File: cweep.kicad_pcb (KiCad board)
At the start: 2 copper layers, 35 parts, among them SW1 SW_Push, SW10 SW_Push, SW11 SW_Push, SW12 SW_Push, SW13 SW_Push, SW14 SW_Push, SW15 SW_Push, SW16 SW_Push, SW17 SW_Push, SW2 SW_Push, SW3 SW_Push, SW4 SW_Push, SW5 SW_Push, SW6 SW_Push, SW7 SW_Push, SW8 SW_Push, SW9 SW_Push, U1 XIAO-nRF52840

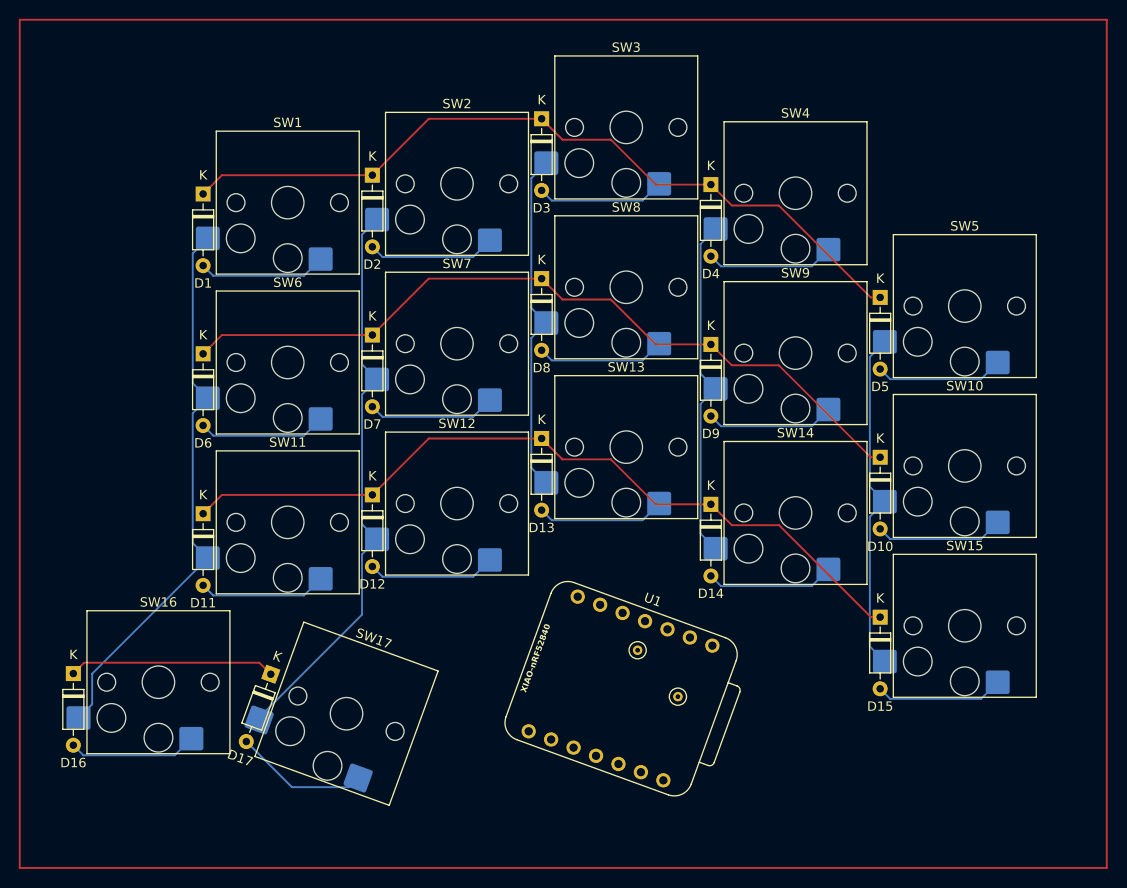
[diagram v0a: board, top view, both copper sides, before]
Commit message: refactor: update footprints
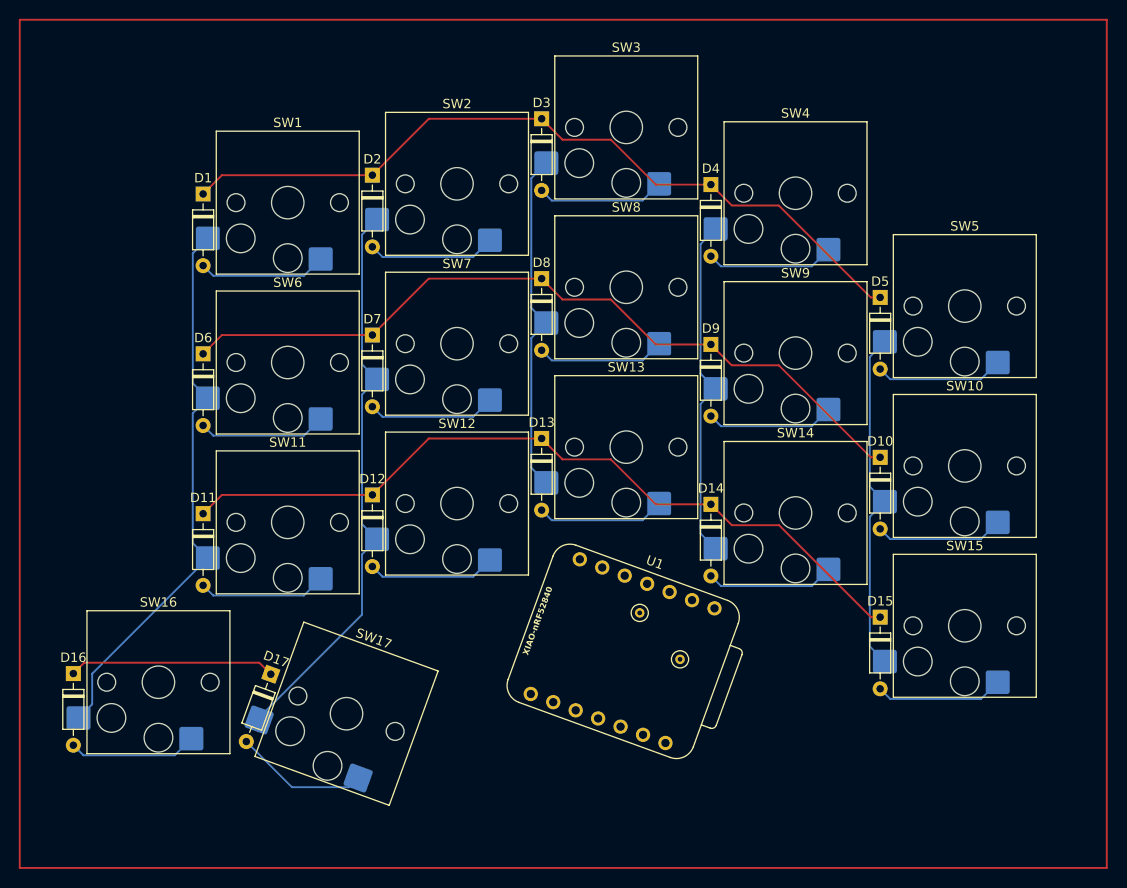
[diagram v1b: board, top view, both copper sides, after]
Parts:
- moved U1 3.98 mm to (222.6, 98.8)

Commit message: feat: add matrix-to-mcu routes
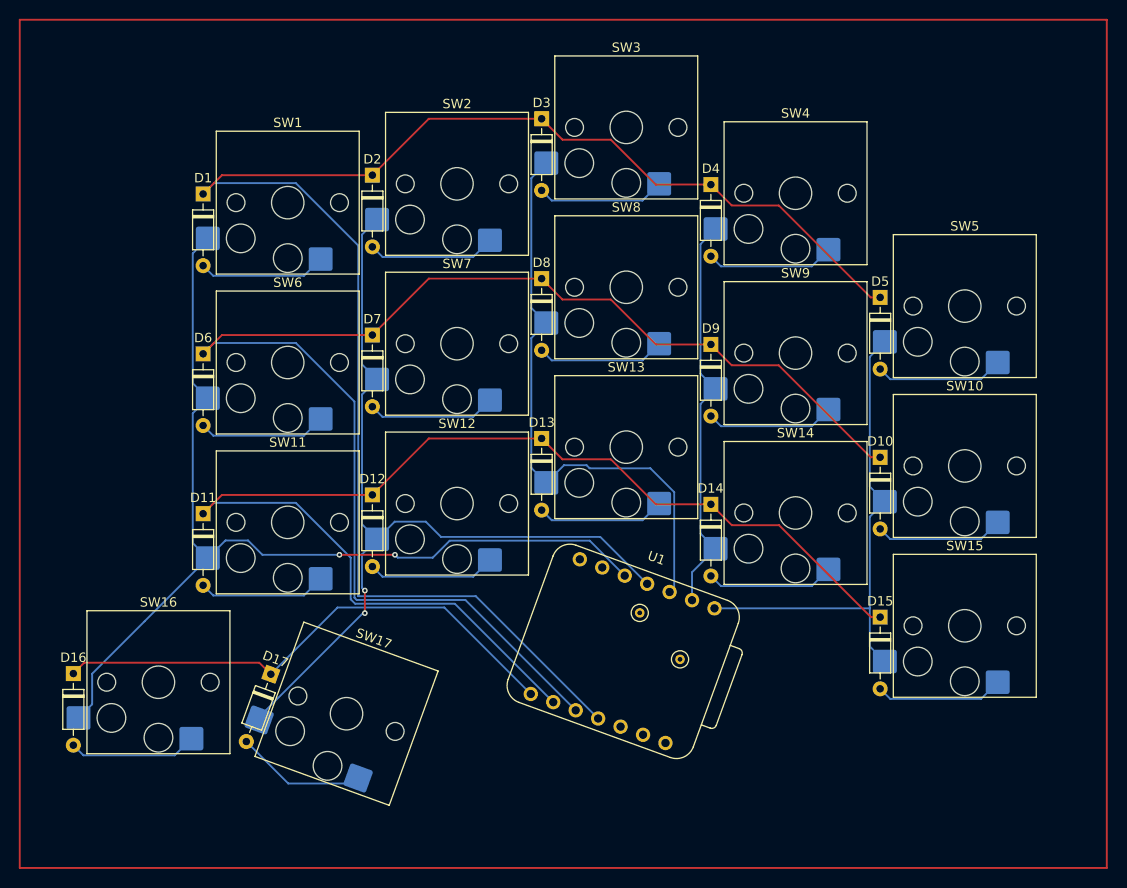
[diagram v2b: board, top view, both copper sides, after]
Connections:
- U1 pad 1: /column 0 -> /column 4
- U1 pad 10: /row 2 -> /row 1
- U1 pad 11: /row 3 -> /row 0
- U1 pad 2: /column 1 -> /column 3
- U1 pad 4: /column 3 -> /column 1
- U1 pad 5: /column 4 -> /column 0
- U1 pad 8: /row 0 -> /row 3
- U1 pad 9: /row 1 -> /row 2
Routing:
- net /row 0: track 83.2 -> 171.1 mm
- net /row 1: track 83.2 -> 151.7 mm
- net /row 2: track 83.2 -> 132.3 mm
- net /column 0: track 59.3 -> 107.5 mm, vias 0 -> 2
- net /row 3: track 22.0 -> 56.4 mm
- net /column 1: track 61.1 -> 93.7 mm, vias 0 -> 2
- net /column 2: track 36.7 -> 63.0 mm
- net /column 4: track 36.7 -> 53.2 mm
- net /column 3: track 36.7 -> 43.2 mm

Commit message: feat: add solar charging circuit
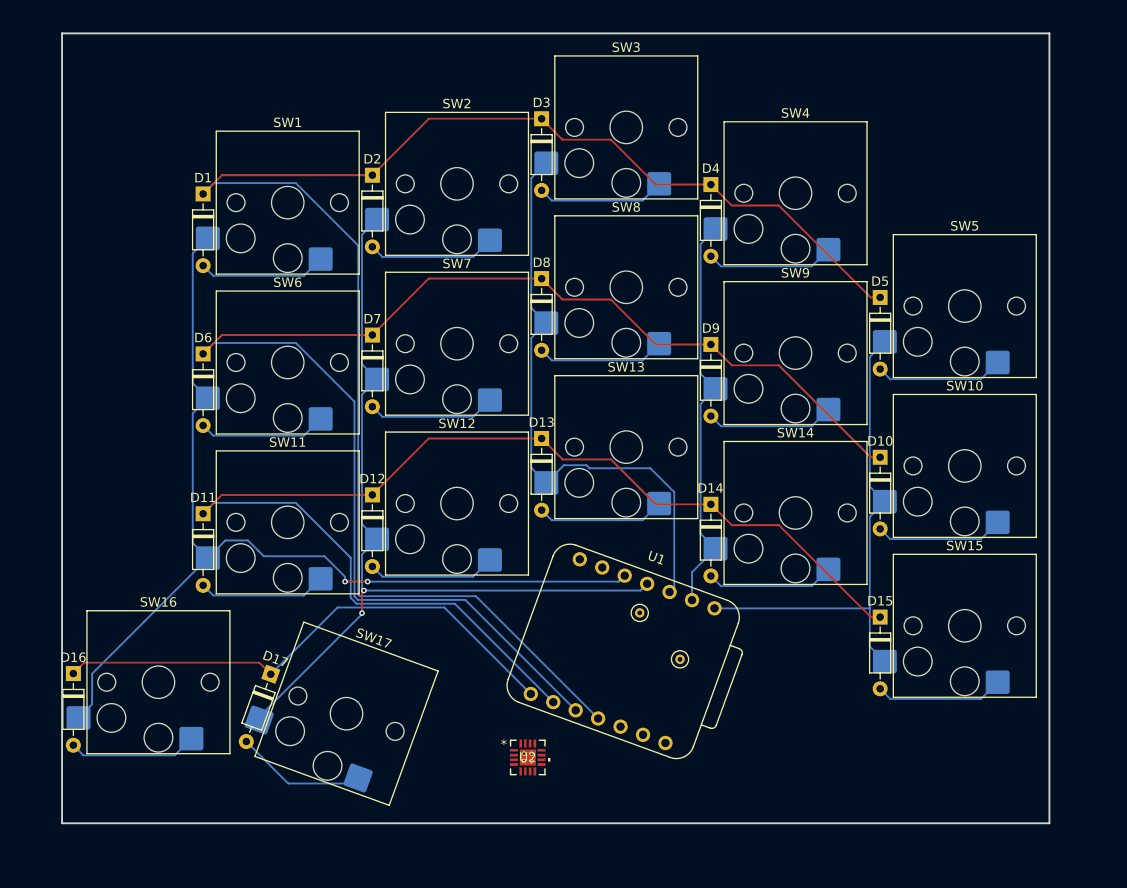
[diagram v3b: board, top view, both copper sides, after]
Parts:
- added U2: BQ25504RGTR, BQ25504RGTR:RGT16_1P7X1P7, F.Cu at (212.5, 110.0)
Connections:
- U1 pad 13: unconnected-(U1-GND-Pad13) -> /GND
- U1 pad 15: unconnected-(U1-BAT-Pad15) -> Net-(BT1-+)
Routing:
- net /column 1: track 93.7 -> 91.9 mm
- net /column 0: track 107.5 -> 106.8 mm
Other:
- board outline added: 105 x 84 mm

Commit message: feat: add solar footprint and models
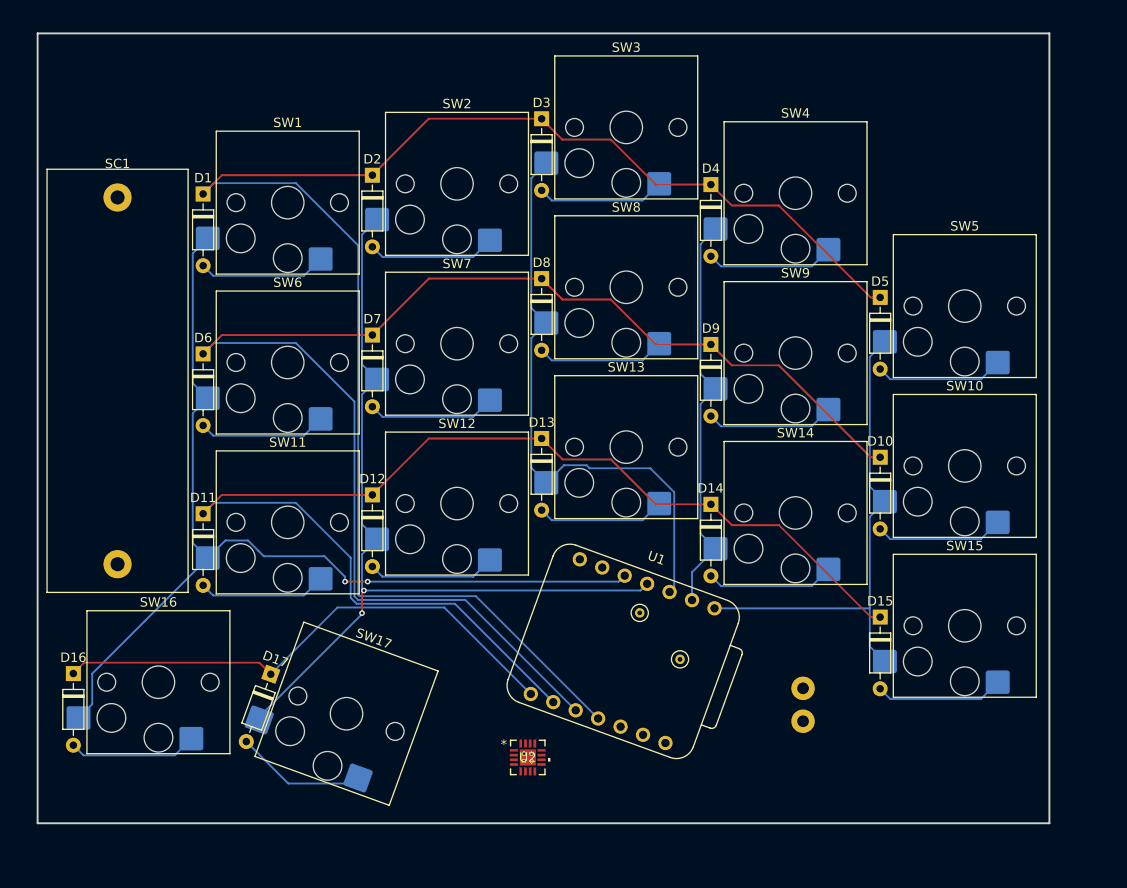
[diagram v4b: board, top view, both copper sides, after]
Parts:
- added BAT+1: MountingHole_Pad, TOTEM:BatteryPad, F.Cu at (241.8, 102.7)
- added BAT-1: MountingHole_Pad, TOTEM:BatteryPad, F.Cu at (241.8, 106.2)
- added SC1: SM141K04LV, cweep:SM141K04LV, F.Cu at (161.1, 92.8)
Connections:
- SW1 pad 1: Net-(D1-A) -> /column 0
- SW1 pad 2: /column 0 -> Net-(D1-A)
- SW10 pad 1: Net-(D10-A) -> /column 4
- SW10 pad 2: /column 4 -> Net-(D10-A)
- SW11 pad 1: Net-(D11-A) -> /column 0
- SW11 pad 2: /column 0 -> Net-(D11-A)
- SW12 pad 1: Net-(D12-A) -> /column 1
- SW12 pad 2: /column 1 -> Net-(D12-A)
- SW13 pad 1: Net-(D13-A) -> /column 2
- SW13 pad 2: /column 2 -> Net-(D13-A)
- SW14 pad 1: Net-(D14-A) -> /column 3
- SW14 pad 2: /column 3 -> Net-(D14-A)
- SW15 pad 1: Net-(D15-A) -> /column 4
- SW15 pad 2: /column 4 -> Net-(D15-A)
- SW16 pad 1: Net-(D16-A) -> /column 0
- SW16 pad 2: /column 0 -> Net-(D16-A)
- SW17 pad 1: Net-(D17-A) -> /column 1
- SW17 pad 2: /column 1 -> Net-(D17-A)
- SW2 pad 1: Net-(D2-A) -> /column 1
- SW2 pad 2: /column 1 -> Net-(D2-A)
- SW3 pad 1: Net-(D3-A) -> /column 2
- SW3 pad 2: /column 2 -> Net-(D3-A)
- SW4 pad 1: Net-(D4-A) -> /column 3
- SW4 pad 2: /column 3 -> Net-(D4-A)
- SW5 pad 1: Net-(D5-A) -> /column 4
- SW5 pad 2: /column 4 -> Net-(D5-A)
- SW6 pad 1: Net-(D6-A) -> /column 0
- SW6 pad 2: /column 0 -> Net-(D6-A)
- SW7 pad 1: Net-(D7-A) -> /column 1
- SW7 pad 2: /column 1 -> Net-(D7-A)
- SW8 pad 1: Net-(D8-A) -> /column 2
- SW8 pad 2: /column 2 -> Net-(D8-A)
- SW9 pad 1: Net-(D9-A) -> /column 3
- SW9 pad 2: /column 3 -> Net-(D9-A)
- U1 pad 13: /GND -> GND
- U1 pad 15: Net-(BT1-+) -> /BAT+
- U2 pad 1: unconnected-(U2-VSS-Pad1) -> GND
- U2 pad 10: unconnected-(U2-OK_PROG-Pad10) -> GND
- U2 pad 12: unconnected-(U2-AVSS-Pad12) -> GND
- U2 pad 13: unconnected-(U2-VSS-Pad13) -> GND
- U2 pad 14: unconnected-(U2-VBAT-Pad14) -> /BAT+
- U2 pad 15: unconnected-(U2-VSTOR-Pad15) -> Net-(U2-VSTOR)
- U2 pad 16: unconnected-(U2-LBST-Pad16) -> Net-(U2-LBST)
- U2 pad 17: unconnected-(U2-EPAD-Pad17) -> GND
- U2 pad 2: unconnected-(U2-VIN_DC-Pad2) -> Net-(SC1-+)
- U2 pad 3: unconnected-(U2-VOC_SAMP-Pad3) -> Net-(U2-VOC_SAMP)
- U2 pad 4: unconnected-(U2-VREF_SAMP-Pad4) -> Net-(U2-VREF_SAMP)
- U2 pad 5: unconnected-(U2-OT_PROG-Pad5) -> GND
- U2 pad 6: unconnected-(U2-VBAT_OV-Pad6) -> Net-(U2-VBAT_OV)
- U2 pad 7: unconnected-(U2-VRDIV-Pad7) -> Net-(U2-VRDIV)
- U2 pad 8: unconnected-(U2-VBAT_UV-Pad8) -> Net-(U2-VBAT_UV)
- U2 pad 9: unconnected-(U2-OK_HYST-Pad9) -> GND
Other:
- board size 105 x 84 mm -> 107.6 x 84 mm

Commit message: feat: add battery
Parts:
- removed BAT+1, BAT-1: MountingHole_Pad, TOTEM:BatteryPad
- added BT1: 3.7V LiPo, cweep:battery-13853-sparkfun-25x15x4, F.Cu at (238.8, 100.2)
- D1, D10, D11, D12, D13, D14, D15, D16, D17, D2, D3, D4, D5, D6, D7, D8, D9: footprint cweep:D_DO-35_SOD27_P7.62mm_Horizontal -> Diode_THT:D_DO-35_SOD27_P7.62mm_Horizontal; moved to B.Cu
- U2: moved to B.Cu
- moved U2 57.3 mm to (171.3, 70.2), turned to 180 degrees
- moved D17 15.8 mm to (196.2, 100.8)
- moved D1 15.7 mm to (188.4, 46.3)
- moved D11 15.7 mm to (188.4, 80.3)
- moved D12 15.7 mm to (206.4, 78.3)
- moved D14 15.7 mm to (242.4, 79.3)
- moved D2 15.7 mm to (206.4, 44.3)
- moved D3 15.7 mm to (224.4, 38.3)
- moved D4 15.7 mm to (242.4, 45.3)
- moved D6 15.7 mm to (188.4, 63.3)
- moved D7 15.7 mm to (206.4, 61.3)
- moved D9 15.7 mm to (242.4, 62.3)
- moved D16 15.5 mm to (174.3, 97.3)
- moved D13 15.2 mm to (224.4, 73.0), turned to -2 degrees
- moved D8 15.2 mm to (224.4, 56.0), turned to -2 degrees
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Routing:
- net /row 0: track 171.0 -> 0.00 mm
- net /row 1: track 151.6 -> 0.00 mm
- net /row 2: track 132.2 -> 0.00 mm
- net /column 0: track 106.8 -> 0.00 mm, vias 2 -> 0
- net /column 1: track 91.9 -> 0.00 mm, vias 2 -> 0
- net /column 2: track 63.0 -> 0.00 mm
- net /row 3: track 56.4 -> 0.00 mm
- net /column 4: track 53.2 -> 0.00 mm
- net /column 3: track 43.2 -> 0.00 mm
- net Net-(D17-A): track 14.0 -> 0.00 mm
- net Net-(D16-A): track 13.7 -> 0.00 mm
- net Net-(D4-A): track 13.7 -> 0.00 mm
- net Net-(D3-A): track 13.7 -> 0.00 mm
- net Net-(D2-A): track 13.7 -> 0.00 mm
- net Net-(D1-A): track 13.7 -> 0.00 mm
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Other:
- board size 107.6 x 84 mm -> 105.2 x 82.3 mm
- board text added: "put reset button here"

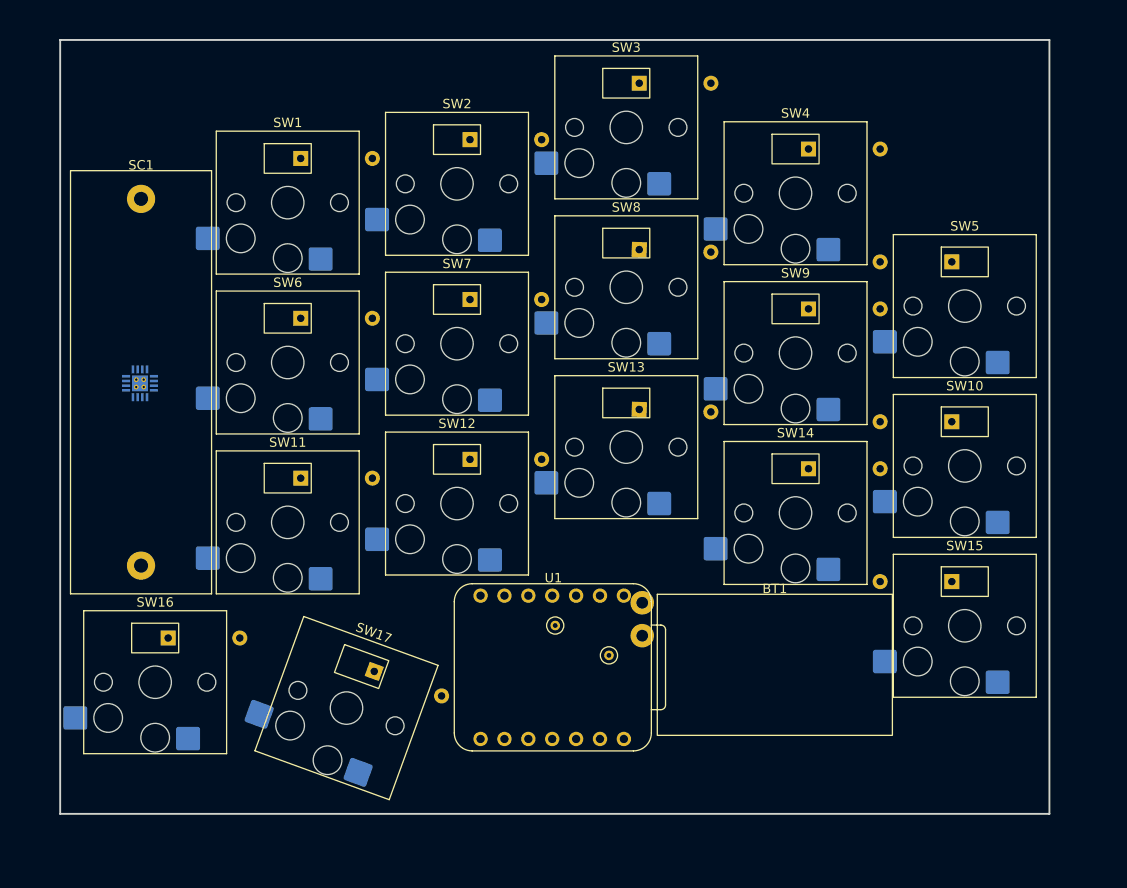
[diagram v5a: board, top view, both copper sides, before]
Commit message: refactor: add R/L suffix
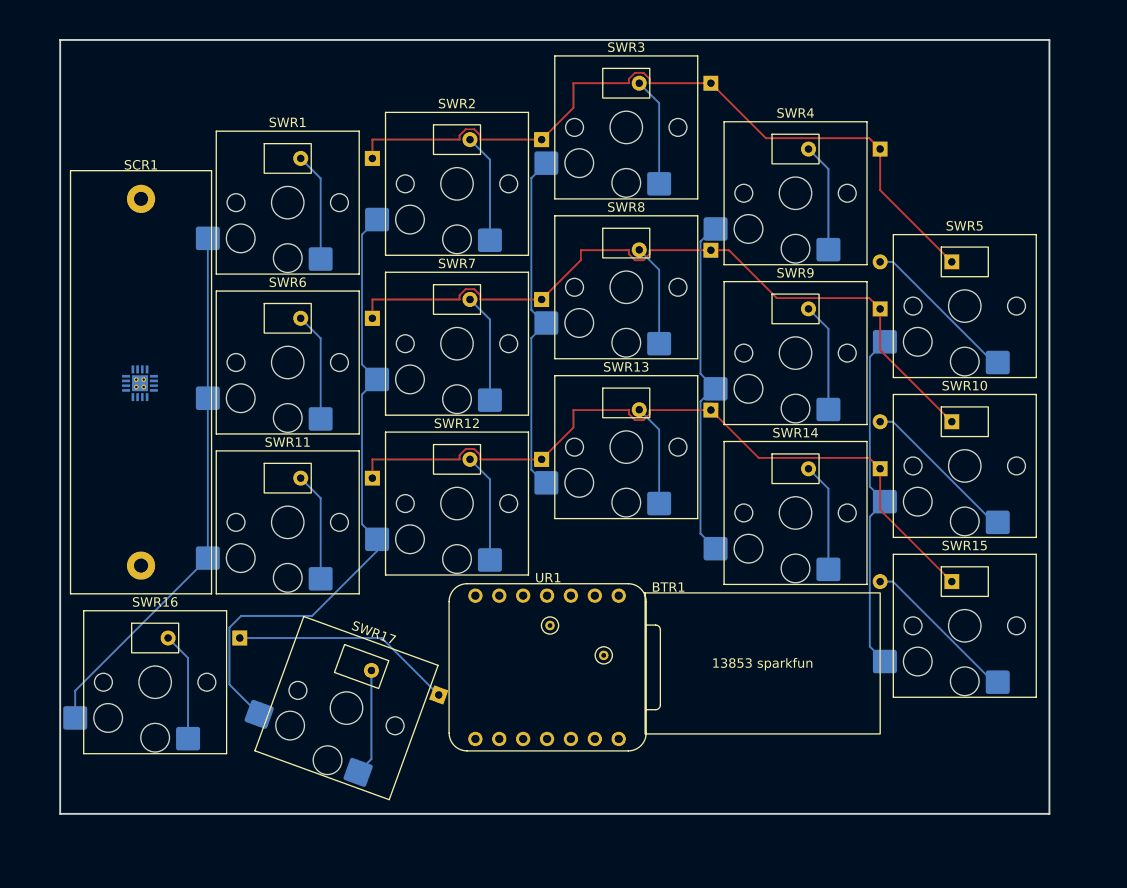
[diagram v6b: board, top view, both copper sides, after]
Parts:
- BTR1: renamed from BT1; value 3.7V LiPo -> 13853 sparkfun; footprint cweep:battery-13853-sparkfun-25x15x4 -> cweep:13853-sparkfun
- moved DR13 7.62 mm to (232.0, 73.1), turned to 179.7 degrees
- moved DR8 7.62 mm to (232.0, 56.1), turned to 179.7 degrees
- moved DR1 7.62 mm to (196.0, 46.3), turned to 180 degrees
- moved DR11 7.62 mm to (196.0, 80.3), turned to 180 degrees
- moved DR12 7.62 mm to (214.0, 78.3), turned to 180 degrees
- moved DR14 7.62 mm to (250.0, 79.3), turned to 180 degrees
- moved DR16 7.62 mm to (181.9, 97.3), turned to 180 degrees
- moved DR2 7.62 mm to (214.0, 44.3), turned to 180 degrees
- moved DR3 7.62 mm to (232.0, 38.3), turned to 180 degrees
- moved DR4 7.62 mm to (250.0, 45.3), turned to 180 degrees
- moved DR6 7.62 mm to (196.0, 63.3), turned to 180 degrees
- moved DR7 7.62 mm to (214.0, 61.3), turned to 180 degrees
- moved DR9 7.62 mm to (250.0, 62.3), turned to 180 degrees
- moved DR17 7.30 mm to (203.1, 103.4), turned to 160 degrees
- moved BTR1 1.31 mm to (237.5, 100.0)
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- renumbered D1 to DR1, D10 to DR10, D11 to DR11, D12 to DR12, D13 to DR13, D14 to DR14, D15 to DR15, D16 to DR16, D17 to DR17, D2 to DR2, D3 to DR3, D4 to DR4, D5 to DR5, D6 to DR6, D7 to DR7, D8 to DR8, D9 to DR9, SC1 to SCR1, SW1 to SWR1, SW10 to SWR10, SW11 to SWR11, SW12 to SWR12, SW13 to SWR13, SW14 to SWR14, SW15 to SWR15, SW16 to SWR16, SW17 to SWR17, SW2 to SWR2, SW3 to SWR3, SW4 to SWR4, SW5 to SWR5, SW6 to SWR6, SW7 to SWR7, SW8 to SWR8, SW9 to SWR9, U1 to UR1, U2 to UR2
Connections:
- net /column 0 renamed /column r0
- net /column 1 renamed /column r1
- net /column 2 renamed /column r2
- net /column 3 renamed /column r3
- net /column 4 renamed /column r4
- net /row 0 renamed /row r0
- net /row 1 renamed /row r1
- net /row 2 renamed /row r2
- net /row 3 renamed /row r3
- UR1 pad 15: /BAT+ -> /BATR+
- UR2 pad 14: /BAT+ -> /BATR+
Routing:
- net /row r0: track 0.00 -> 81.0 mm
- net /row r2: track 0.00 -> 79.8 mm
- net /row r1: track 0.00 -> 79.3 mm
- net /column r1: track 0.00 -> 67.5 mm
- net /column r0: track 0.00 -> 56.8 mm
- net /column r3: track 0.00 -> 37.0 mm
- net /column r2: track 0.00 -> 36.9 mm
- net /column r4: track 0.00 -> 36.7 mm
- net /row r3: track 0.00 -> 23.7 mm
- net Net-(DR5-A): track 0.00 -> 16.9 mm
- net Net-(DR15-A): track 0.00 -> 16.9 mm
- net Net-(DR10-A): track 0.00 -> 16.9 mm
- net Net-(DR9-A): track 0.00 -> 11.6 mm
- net Net-(DR7-A): track 0.00 -> 11.6 mm
- net Net-(DR6-A): track 0.00 -> 11.6 mm
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
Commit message: feat: add matrix traces
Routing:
- net /row r0: track 81.0 -> 173.6 mm
- net /column r0: track 56.8 -> 143.3 mm
- net /row r1: track 79.3 -> 157.9 mm
- net /row r2: track 79.8 -> 142.5 mm
- net /column r4: track 36.7 -> 67.9 mm
- net /column r1: track 67.5 -> 88.9 mm
- net /column r2: track 36.9 -> 49.8 mm
- net /row r3: track 23.7 -> 30.0 mm
- net /column r3: track 37.0 -> 33.4 mm
